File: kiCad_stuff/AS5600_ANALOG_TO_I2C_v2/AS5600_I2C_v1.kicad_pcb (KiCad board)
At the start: 2 copper layers, 25 x 19 mm, 10 parts, among them J1 Conn_01x04, U2 MCP3221

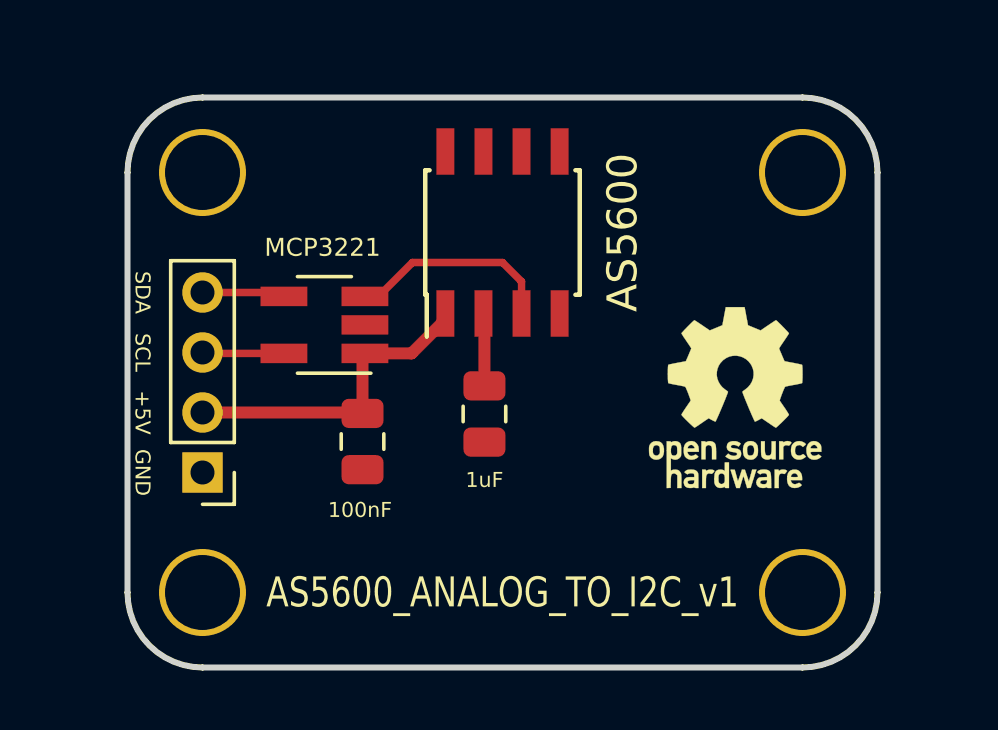
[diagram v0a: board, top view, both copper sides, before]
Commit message: Tweaking encoder PCB dimensions
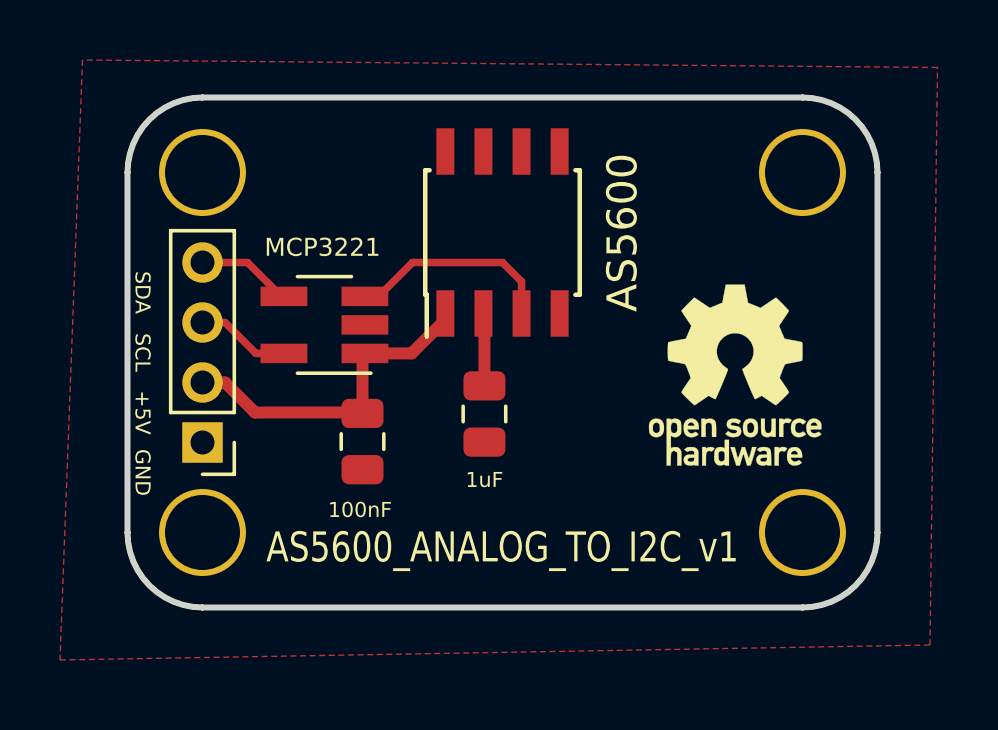
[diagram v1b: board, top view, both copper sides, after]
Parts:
- 2.5mm : value Hole_BR -> Hole_BL
- moved 2.5mm  2.00 mm to (172.0, 61.0)
- moved J1 1.00 mm to (152.0, 68.0)
- moved REF** 0.75 mm to (169.8, 65.8)
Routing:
- net SDA: track 2.77 -> 3.37 mm
- added copper zone on F.Cu, net GND
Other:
- board size 25 x 19 mm -> 25 x 17 mm
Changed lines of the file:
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@@
   (general
     (thickness 1.6)
-    (drawings 13)
-    (tracks 18)
+    (drawings 15)
+    (tracks 23)
     (zones 0)
     (modules 10)
@@
     (mod_text_size 1 1)
     (mod_text_width 0.15)
-    (pad_size 1.5 1.5)
-    (pad_drill 1)
+    (pad_size 2.9 2.9)
+    (pad_drill 2.5)
     (pad_to_mask_clearance 0.2)
     (aux_axis_origin 0 0)
@@
     (add_net SDA)
   )
+  (module modular_segment_PCB_footprints:MountingHole_2.5mm_Pad (layer F.Cu)
+    (at 172 61)
+    (descr "Mounting Hole 2.5mm")
+    (tags "mounting hole 2.5mm")
+    (attr virtual)
+    (fp_text reference "2.5mm " (at 0.5 4) (layer F.SilkS) hide
+      (effects (font (size 1 1) (thickness 0.15)))
+    )
+    (fp_text value Hole_BL (at 6.5 3.5) (layer F.Fab) hide
+      (effects (font (size 1 1) (thickness 0.15)))
+    )
+    (pad "" np_thru_hole circle (at 0 -2) (size 2.9 2.9) (drill 2.5) (layers *.Cu *.Mask))
+  )
   (module Symbol:OSHW-Logo_5.7x6mm_SilkScreen (layer F.Cu)
-    (at 169.75 66.5)
+    (at 169.75 65.75)
     (descr "Open Source Hardware Logo")
     (tags "Logo OSHW")
@@
   )
   (module Connector_PinHeader_2.00mm:PinHeader_1x04_P2.00mm_Vertical (layer F.Cu)
-    (at 152 69 180)
+    (at 152 68 180)
     (descr "Through hole straight pin header, 1x04, 2.00mm pitch, single row")
     (tags "Through hole pin header THT 1x04 2.00mm single row")
@@
     (pad "" np_thru_hole circle (at 0 0) (size 2.9 2.9) (drill 2.5) (layers *.Cu *.Mask))
   )
-  (module modular_segment_PCB_footprints:MountingHole_2.5mm_Pad locked (layer F.Cu)
-    (at 172 59)
-    (descr "Mounting Hole 2.5mm")
-    (tags "mounting hole 2.5mm")
-    (attr virtual)
-    (fp_text reference "2.5mm " (at 4.5 -3) (layer F.SilkS) hide
-      (effects (font (size 1 1) (thickness 0.15)))
-    )
-    (fp_text value Hole_BR (at 6.5 0) (layer F.Fab) hide
-      (effects (font (size 1 1) (thickness 0.15)))
-    )
-    (pad "" np_thru_hole circle (at 0 0) (size 2.9 2.9) (drill 2.5) (layers *.Cu *.Mask))
-  )
   (module Package_TO_SOT_SMD:SOT-23-5_HandSoldering (layer F.Cu)
     (at 156.064 64.08 180)
@@
       (effects (font (size 1 1) (thickness 0.15)))
     )
-    (fp_text value AS5600_ANALOG_TO_I2C_v1 (at -12 0 180) (layer F.SilkS)
+    (fp_text value AS5600_ANALOG_TO_I2C_v1 (at -10.5 0 180) (layer F.SilkS)
       (effects (font (size 1 0.8) (thickness 0.1)))
     )
@@
       (effects (font (size 1 1) (thickness 0.15)))
     )
-    (pad "" np_thru_hole circle (at 0 0) (size 2.9 2.9) (drill 2.5) (layers *.Cu *.Mask))
+    (pad "" np_thru_hole circle (at 0 -2) (size 2.9 2.9) (drill 2.5) (layers *.Cu *.Mask)
+      (zone_connect 2))
   )
   (module modular_segment_PCB_footprints:MountingHole_2.5mm_Pad (layer F.Cu)
@@
       (effects (font (size 1 1) (thickness 0.15)))
     )
-    (pad "" np_thru_hole circle (at 0 0) (size 2.9 2.9) (drill 2.5) (layers *.Cu *.Mask))
+    (pad "" np_thru_hole circle (at 0 -2) (size 2.9 2.9) (drill 2.5) (layers *.Cu *.Mask))
+  )
+  (dimension 12 (width 0.3) (layer Dwgs.User)
+    (gr_text "12.000 mm" (at 180.6 65 270) (layer Dwgs.User)
+      (effects (font (size 1.5 1.5) (thickness 0.3)))
+    )
+    (feature1 (pts (xy 172 71) (xy 179.086421 71)))
+    (feature2 (pts (xy 172 59) (xy 179.086421 59)))
+    (crossbar (pts (xy 178.5 59) (xy 178.5 71)))
+    (arrow1a (pts (xy 178.5 71) (xy 177.913579 69.873496)))
+    (arrow1b (pts (xy 178.5 71) (xy 179.086421 69.873496)))
+    (arrow2a (pts (xy 178.5 59) (xy 177.913579 60.126504)))
+    (arrow2b (pts (xy 178.5 59) (xy 179.086421 60.126504)))
+  )
+  (dimension 20 (width 0.3) (layer Dwgs.User)
+    (gr_text "20.000 mm" (at 162 50.4) (layer Dwgs.User)
+      (effects (font (size 1.5 1.5) (thickness 0.3)))
+    )
+    (feature1 (pts (xy 172 59) (xy 172 51.913579)))
+    (feature2 (pts (xy 152 59) (xy 152 51.913579)))
+    (crossbar (pts (xy 152 52.5) (xy 172 52.5)))
+    (arrow1a (pts (xy 172 52.5) (xy 170.873496 53.086421)))
+    (arrow1b (pts (xy 172 52.5) (xy 170.873496 51.913579)))
+    (arrow2a (pts (xy 152 52.5) (xy 153.126504 53.086421)))
+    (arrow2b (pts (xy 152 52.5) (xy 153.126504 51.913579)))
   )
   (gr_arc (start 172 59) (end 174.5 59) (angle -90) (layer Edge.Cuts) (width 0.2))
-  (gr_arc (start 172 73) (end 172 75.5) (angle -90) (layer Edge.Cuts) (width 0.2))
-  (gr_arc (start 152 73) (end 149.5 73) (angle -90) (layer Edge.Cuts) (width 0.2))
+  (gr_arc (start 172 71) (end 172 73.5) (angle -90) (layer Edge.Cuts) (width 0.2))
+  (gr_arc (start 152 71) (end 149.5 71) (angle -90) (layer Edge.Cuts) (width 0.2))
   (gr_arc (start 152 59) (end 152 56.5) (angle -90) (layer Edge.Cuts) (width 0.2))
   (gr_line (start 172 56.5) (end 152 56.5) (layer Edge.Cuts) (width 0.2))
-  (gr_line (start 174.5 73) (end 174.5 59) (layer Edge.Cuts) (width 0.2))
-  (gr_line (start 152 75.5) (end 172 75.5) (layer Edge.Cuts) (width 0.2))
-  (gr_line (start 149.5 59) (end 149.5 73) (layer Edge.Cuts) (width 0.2))
+  (gr_line (start 174.5 71) (end 174.5 59) (layer Edge.Cuts) (width 0.2))
+  (gr_line (start 152 73.5) (end 172 73.5) (layer Edge.Cuts) (width 0.2))
+  (gr_line (start 149.5 59) (end 149.5 71) (layer Edge.Cuts) (width 0.2))
   (gr_text "2.5mm\n" (at 172 70.75) (layer Dwgs.User)
     (effects (font (size 0.5 0.5) (thickness 0.125)))
@@
   (segment (start 160.095 63.7) (end 160.095 63.905) (width 0.4) (layer F.Cu) (net 1))
   (segment (start 160.095 63.905) (end 158.97 65.03) (width 0.4) (layer F.Cu) (net 1))
-  (segment (start 157.303 67) (end 157.334 67.031) (width 0.4) (layer F.Cu) (net 1))
-  (segment (start 152 67) (end 157.303 67) (width 0.4) (layer F.Cu) (net 1))
   (segment (start 157.334 65.11) (end 157.414 65.03) (width 0.4) (layer F.Cu) (net 1))
   (segment (start 157.334 67.031) (end 157.334 65.11) (width 0.4) (layer F.Cu) (net 1))
+  (segment (start 152.75 66) (end 152 66) (width 0.4) (layer F.Cu) (net 1))
+  (segment (start 153.75 67) (end 152.75 66) (width 0.4) (layer F.Cu) (net 1))
+  (segment (start 157.334 67.031) (end 157.303 67) (width 0.4) (layer F.Cu) (net 1))
+  (segment (start 157.303 67) (end 153.75 67) (width 0.4) (layer F.Cu) (net 1))
   (segment (start 161.398 63.733) (end 161.365 63.7) (width 0.4) (layer F.Cu) (net 3))
   (segment (start 161.398 66.112) (end 161.398 63.733) (width 0.4) (layer F.Cu) (net 3))
   (segment (start 154.584 63) (end 154.714 63.13) (width 0.25) (layer F.Cu) (net 4))
-  (segment (start 152 63) (end 154.584 63) (width 0.25) (layer F.Cu) (net 4))
-  (segment (start 152.03 65.03) (end 152 65) (width 0.25) (layer F.Cu) (net 5))
-  (segment (start 154.714 65.03) (end 152.03 65.03) (width 0.25) (layer F.Cu) (net 5))
+  (segment (start 153.5 62) (end 152 62) (width 0.25) (layer F.Cu) (net 4))
+  (segment (start 154.714 63.13) (end 154.63 63.13) (width 0.25) (layer F.Cu) (net 4))
+  (segment (start 154.63 63.13) (end 153.5 62) (width 0.25) (layer F.Cu) (net 4))
+  (segment (start 153.78 65.03) (end 154.714 65.03) (width 0.25) (layer F.Cu) (net 5))
+  (segment (start 152 64) (end 152.75 64) (width 0.25) (layer F.Cu) (net 5))
+  (segment (start 152.75 64) (end 153.78 65.03) (width 0.25) (layer F.Cu) (net 5))
   (segment (start 162.635 62.635) (end 162.635 63.7) (width 0.25) (layer F.Cu) (net 6))
   (segment (start 162 62) (end 162.635 62.635) (width 0.25) (layer F.Cu) (net 6))
@@
   (segment (start 157.414 63.13) (end 157.869 63.13) (width 0.25) (layer F.Cu) (net 6))
   (segment (start 157.869 63.13) (end 158.999 62) (width 0.25) (layer F.Cu) (net 6))
+  (zone (net 2) (net_name GND) (layer F.Cu) (hatch edge 0.508)
+    (connect_pads yes (clearance 0.35))
+    (min_thickness 0.254)
+    (fill yes (arc_segments 16) (thermal_gap 0.508) (thermal_bridge_width 0.508))
+    (polygon
+      (pts
+        (xy 148 55.25) (xy 147.25 75.25) (xy 176.25 74.75) (xy 176.5 55.5)
+      )
+    )
+  )
 )

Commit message: some minor tweaks
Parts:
- moved 2.5mm  1.00 mm to (172.0, 74.0)
- moved 2.5mm  1.00 mm to (152.0, 74.0)
- moved AS5600 0.50 mm to (162.0, 61.5)
- moved C1 0.50 mm to (157.3, 68.5)
- moved C2 0.50 mm to (161.4, 67.5)
- moved J1 0.50 mm to (152.0, 68.5)
- moved U2 0.50 mm to (156.1, 64.6)
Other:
- board size 25 x 17 mm -> 25 x 18 mm
